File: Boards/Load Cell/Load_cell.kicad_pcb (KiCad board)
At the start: 2 copper layers, 1 part

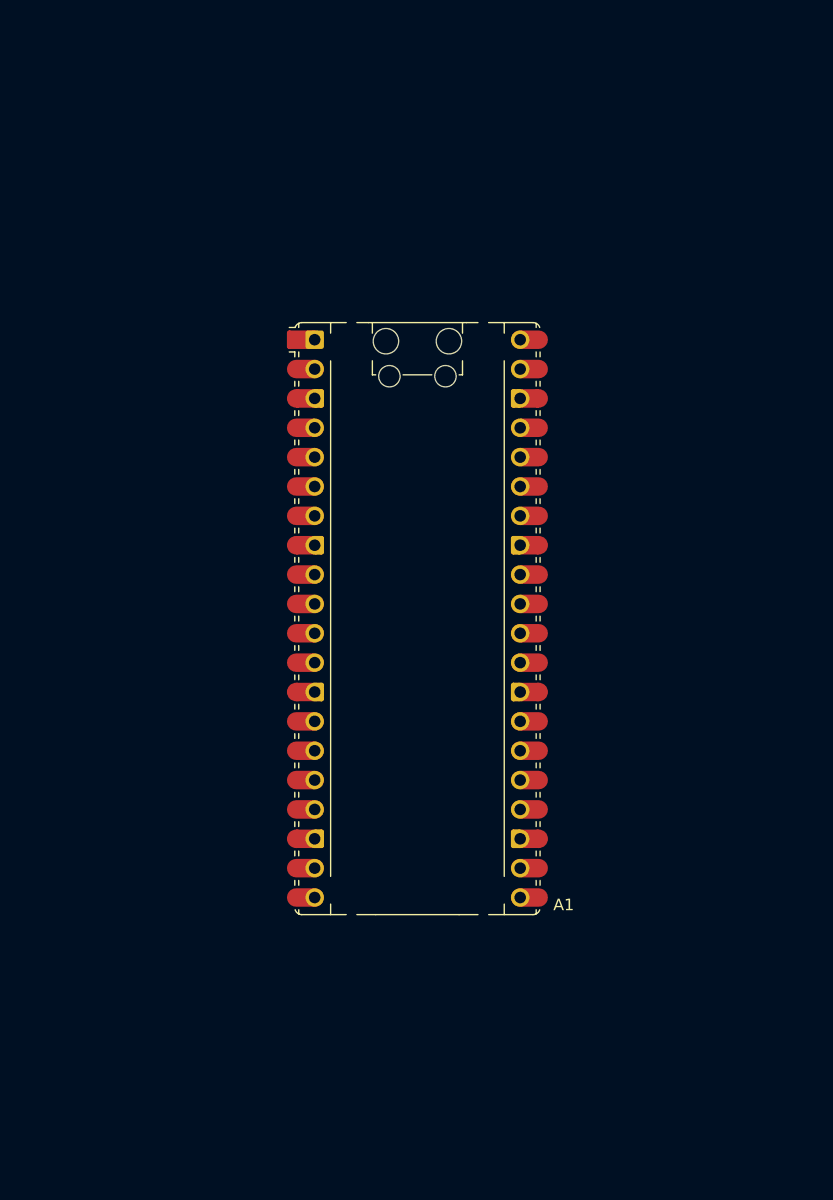
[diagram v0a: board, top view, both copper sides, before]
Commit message: PCB Loadcell
Acabei a PCB Loadcell ( Disposto a mudanças). Vai ser reviewed pelo Alexandre.
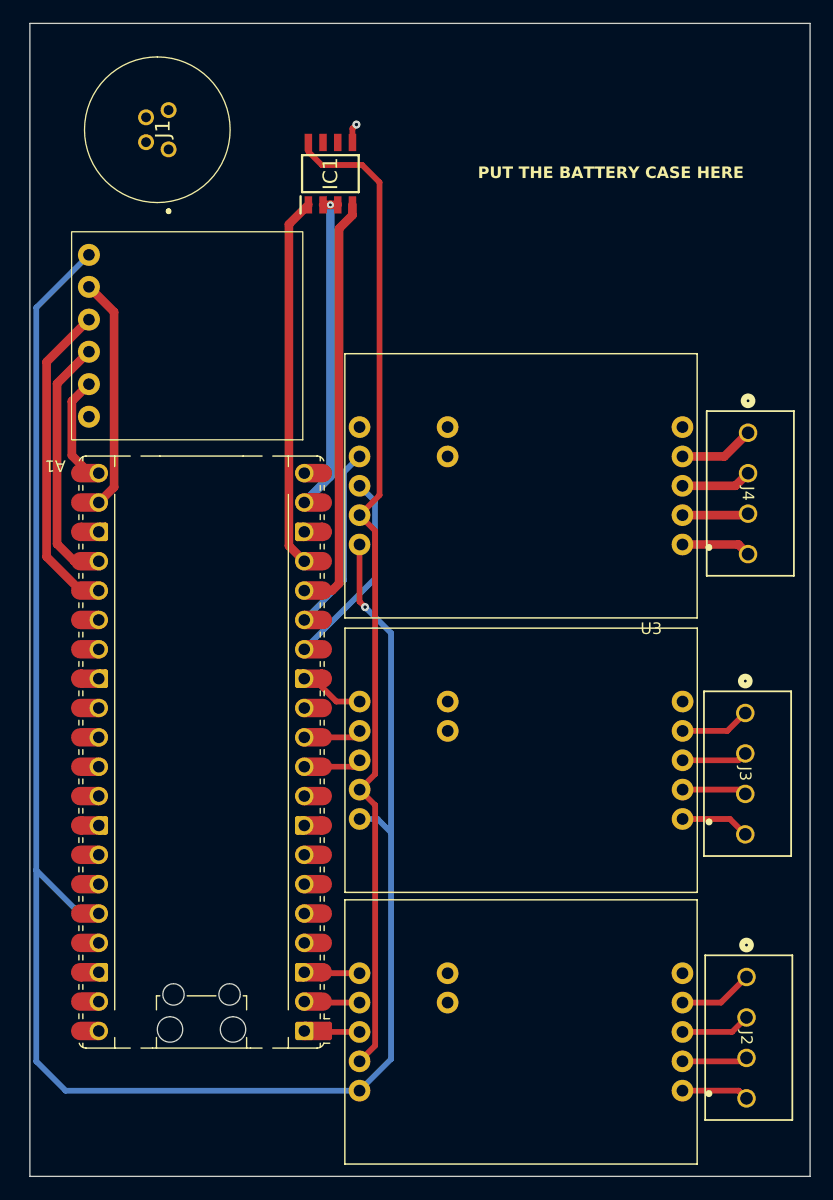
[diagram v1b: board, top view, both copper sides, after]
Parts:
- added IC1: ST1480ABDR, DMP2040USD-13:SOIC127P600X175-8N, F.Cu at (127.4, 41.6)
- added J1: T4040014041-000, T4040014041-000:T4040014041000, F.Cu at (113.4, 39.5)
- added J2: 393570004, 393570004:CONN_SD-39357-001_04P_MOL, F.Cu at (163.4, 111.1)
- added J3: 393570004, 393570004:CONN_SD-39357-001_04P_MOL, F.Cu at (163.3, 88.2)
- added J4: 393570004, 393570004:CONN_SD-39357-001_04P_MOL, F.Cu at (163.5, 64.0)
- added REF**: MicroSDCard, microsdcard:MicroSDCard, F.Cu at (106.5, 48.1)
- added U1: SEN-13879, SEN-13879:SPARKFUN_SEN-13879, F.Cu at (143.8, 115.8)
- added U2: SEN-13879, SEN-13879:SPARKFUN_SEN-13879, F.Cu at (143.9, 92.3)
- added U3: SEN-13879, SEN-13879:SPARKFUN_SEN-13879, F.Cu at (143.8, 68.6)
- moved A1 22.0 mm to (116.2, 91.6), turned to 180 degrees
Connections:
- A1 pad 1: /CLK1 -> /DAT1
- A1 pad 10: /DAT3 -> /DAT2
- A1 pad 11: unconnected-(A1-GPIO8-Pad11) -> /CLK2
- A1 pad 14: unconnected-(A1-GPIO10-Pad14) -> /DAT3
- A1 pad 15: unconnected-(A1-GPIO11-Pad15) -> /CLK3
- A1 pad 16: unconnected-(A1-GPIO12-Pad16) -> /UART TX
- A1 pad 17: unconnected-(A1-GPIO13-Pad17) -> /UART RX
- A1 pad 19: unconnected-(A1-GPIO14-Pad19) -> /Digital Output
- A1 pad 2: /DAT1 -> /CLK1
- A1 pad 21: unconnected-(A1-GPIO16-Pad21) -> /SD MISO
- A1 pad 22: unconnected-(A1-GPIO17-Pad22) -> /SD CS
- A1 pad 24: unconnected-(A1-GPIO18-Pad24) -> /CLK
- A1 pad 25: unconnected-(A1-GPIO19-Pad25) -> /SD MOSI
- A1 pad 5: /CLK2 -> unconnected-(A1-GPIO3-Pad5)
- A1 pad 6: /DAT2 -> unconnected-(A1-GPIO4-Pad6)
- A1 pad 9: /CLK3 -> unconnected-(A1-GPIO6-Pad9)
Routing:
- net /3V3: track 0.00 -> 160.4 mm, vias 0 -> 1
- net /VCC: track 0.00 -> 87.0 mm
- net /UART TX: track 0.00 -> 35.7 mm
- net /UART RX: track 0.00 -> 32.1 mm
- net /Digital Output: track 0.00 -> 28.0 mm, vias 0 -> 1
- net /SD MOSI: track 0.00 -> 27.0 mm
- net /CLK: track 0.00 -> 21.2 mm
- net /SD CS: track 0.00 -> 20.1 mm
- net /DAT3: track 0.00 -> 17.2 mm
- net /CLK3: track 0.00 -> 16.1 mm
- net GND: track 0.00 -> 12.1 mm, vias 0 -> 1
- net /SD MISO: track 0.00 -> 8.95 mm
- net /GRN3: track 0.00 -> 6.52 mm
- net /GRN1: track 0.00 -> 6.46 mm
- net /WHT3: track 0.00 -> 6.13 mm
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- added copper zone on In1.Cu, net GND
- added copper zone on In2.Cu, net GND
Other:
- board outline added: 67.5 x 99.7 mm
- copper layers 2 -> 4
- board text added: "PUT THE BATTERY CASE HERE"

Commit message: PCB Loadcells Acabada
Acabei o design das pcbs das loadcells, so falta colocar os logos e buracos m3.
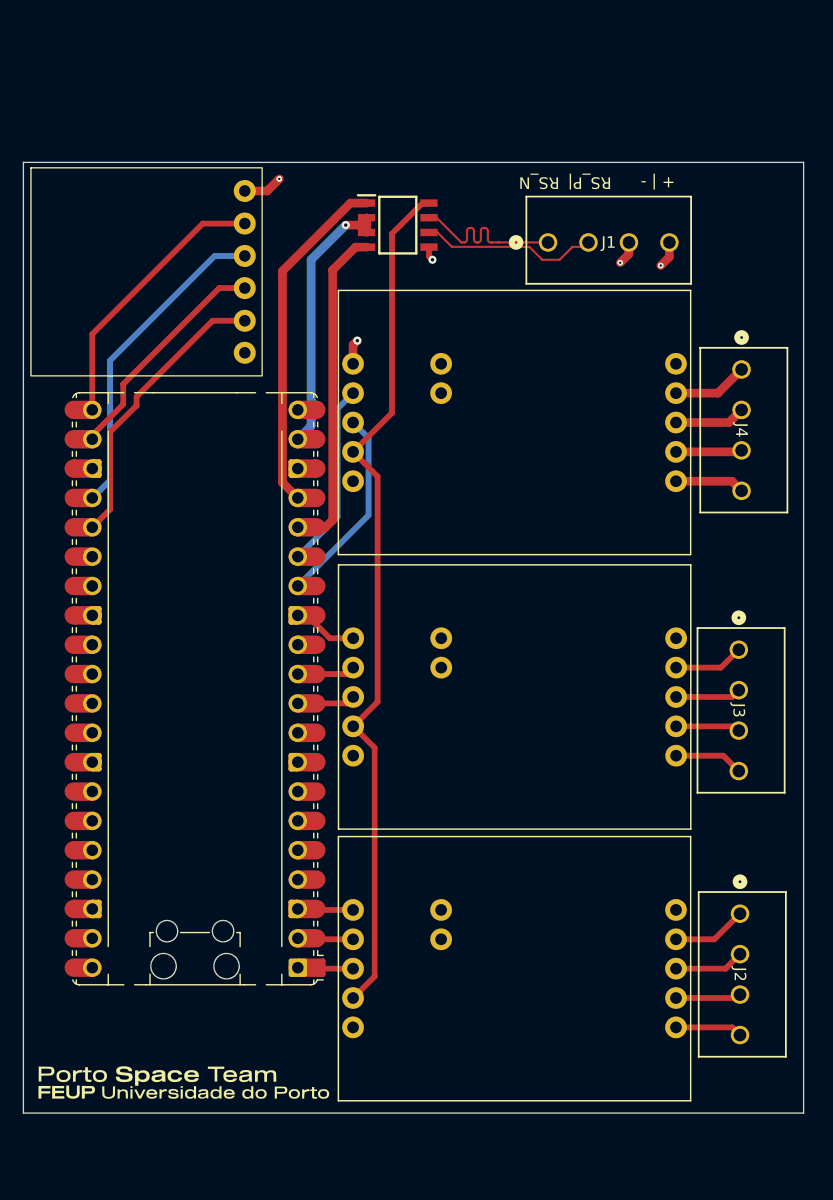
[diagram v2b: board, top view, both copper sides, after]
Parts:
- added G***: LOGO, FEUP-text:Feup-text, F.Cu at (114.7, 120.3)
- J1: value T4040014041-000 -> 393570004; footprint T4040014041-000:T4040014041000 -> 393570004:CONN_SD-39357-001_04P_MOL
- moved J1 33.8 mm to (146.2, 47.5), turned to 0 degrees
- moved REF** 16.5 mm to (120.0, 57.6), turned to 0 degrees
- moved IC1 7.33 mm to (133.2, 46.0), turned to 0 degrees
- moved J2 5.50 mm to (162.8, 105.6)
- moved U2 5.50 mm to (143.3, 86.8)
- moved J4 5.50 mm to (162.9, 58.5)
- moved U3 5.50 mm to (143.3, 63.1)
- moved A1 5.50 mm to (115.7, 86.1)
- moved J3 5.50 mm to (162.7, 82.8)
- moved U1 5.50 mm to (143.3, 110.4)
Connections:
- net /RS B renamed /RS_N
- A1 pad 22: /SD CS -> /SD MOSI
- A1 pad 25: /SD MOSI -> /SD CS
- IC1 pad 6: /RS A -> /RS_P
- J1 pad 2: unconnected-(J1-Pad2) -> /RS_P
- J1 pad 3: /RS A -> GND
- J1 pad 4: unconnected-(J1-Pad4) -> /3V3
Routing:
- net /3V3: track 160.4 -> 2.31 mm
- net /RS_P: track 0.00 -> 15.4 mm
- net /RS_N: track 0.00 -> 15.3 mm
- net /SD MISO: track 8.95 -> 23.7 mm
- net /VCC: track 87.0 -> 75.1 mm
- net /UART TX: track 35.7 -> 27.9 mm
- net GND: track 12.1 -> 19.3 mm, vias 1 -> 4
- net /SD MOSI: track 27.0 -> 19.8 mm
- net /CLK: track 21.2 -> 27.9 mm
- net /SD CS: track 20.1 -> 25.7 mm
- net /Digital Output: track 28.0 -> 23.5 mm
- net /UART RX: track 32.1 -> 29.9 mm
- added copper zone on In1.Cu, net /3V3
- removed copper zone on In1.Cu, net GND
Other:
- board size 67.5 x 99.7 mm -> 67.5 x 82.2 mm
- board text added: "+ | -"
- board text added: "RS_N"
- board text added: "RS_P|"
- board text removed: "PUT THE BATTERY CASE HERE"
